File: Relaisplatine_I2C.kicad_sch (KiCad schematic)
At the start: 74 parts, among them J1 K, J1.1 G1-K, J1.1a1001 G1-J, J1.1a1002 G1-K, J1.1a1003 G1-K, J1.1a1004 G1-K, J1.1a1005 G1-K, J1.1a1006 G1-K, J1.1a1007 G1-K, J1.2 G1-J, J1.2a1001 G1-K, J1.2a1002 G1-J, J1.2a1003 G1-J, J1.2a1004 G1-J, J1.2a1005 G1-J, J1.2a1006 G1-J, J1.2a1007 G1-J, J10 I²C, J11 Relais-Power, J12 Int, J2 J, J2.1 G2-K, J2.1a1001 G1-J, J2.2 G2-J, J2.2a1001 G2-K, J3.1 G3-K, J3.2 G3-J, J4.1 G4-K, J4.2 G4-J, J5.1 G5-K, J5.2 G5-J, J6.1 G6-K, J6.2 G6-J, J7.1 G7-K, J7.2 G7-J, J8.1 G8-K, J8.2 G8-J, U1 ULN2803A, U2 PCF8574

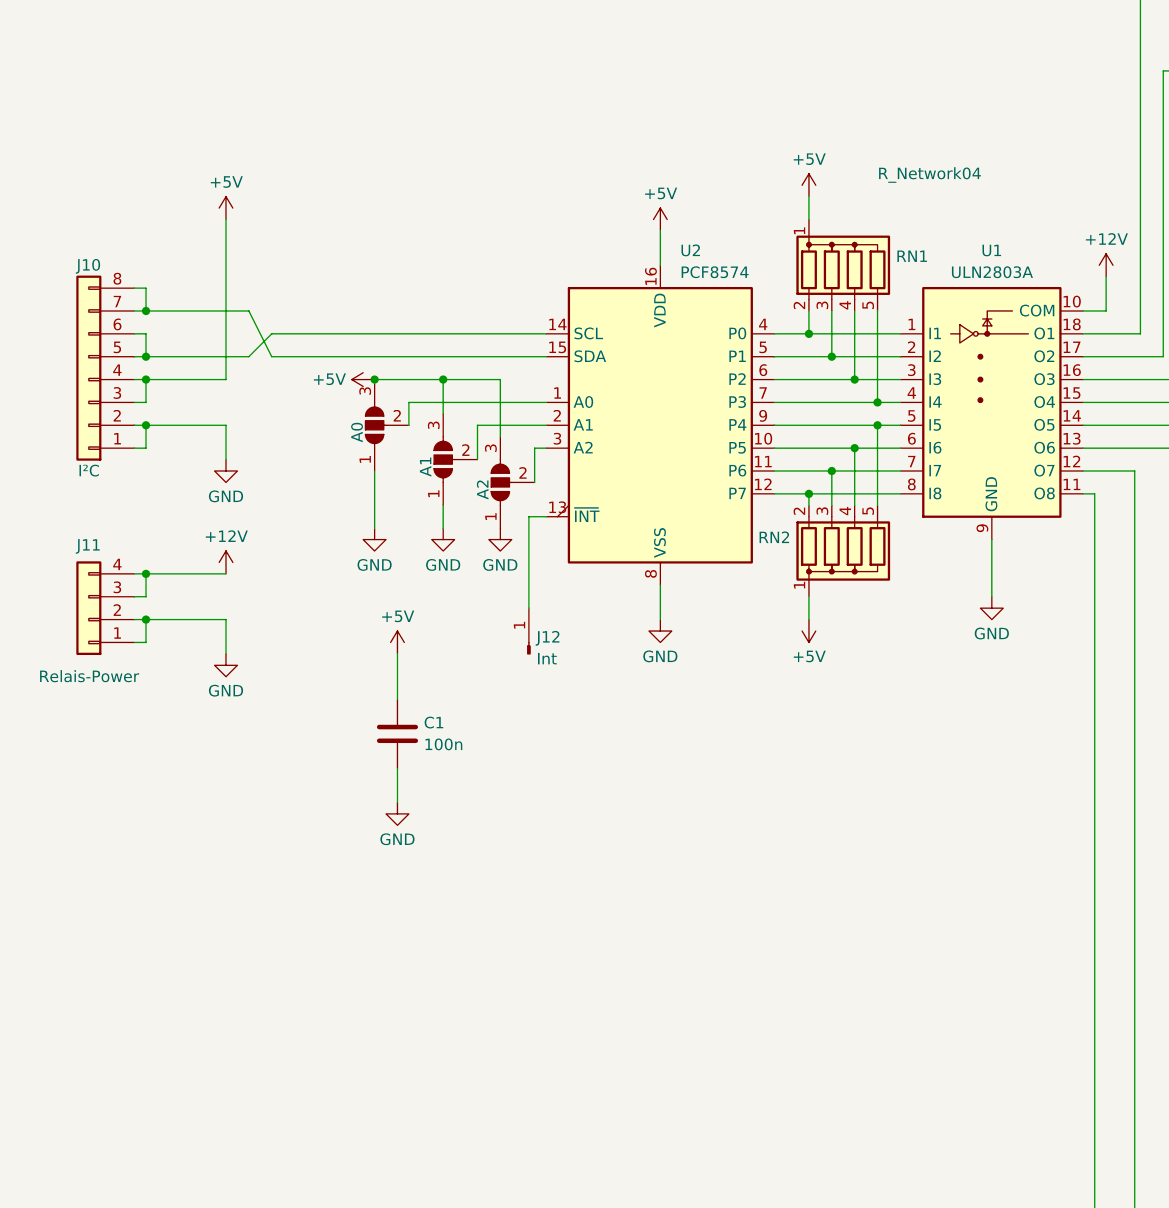
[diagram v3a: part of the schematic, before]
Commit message: Power-LEDs für 5V und 12V hinzugefügt
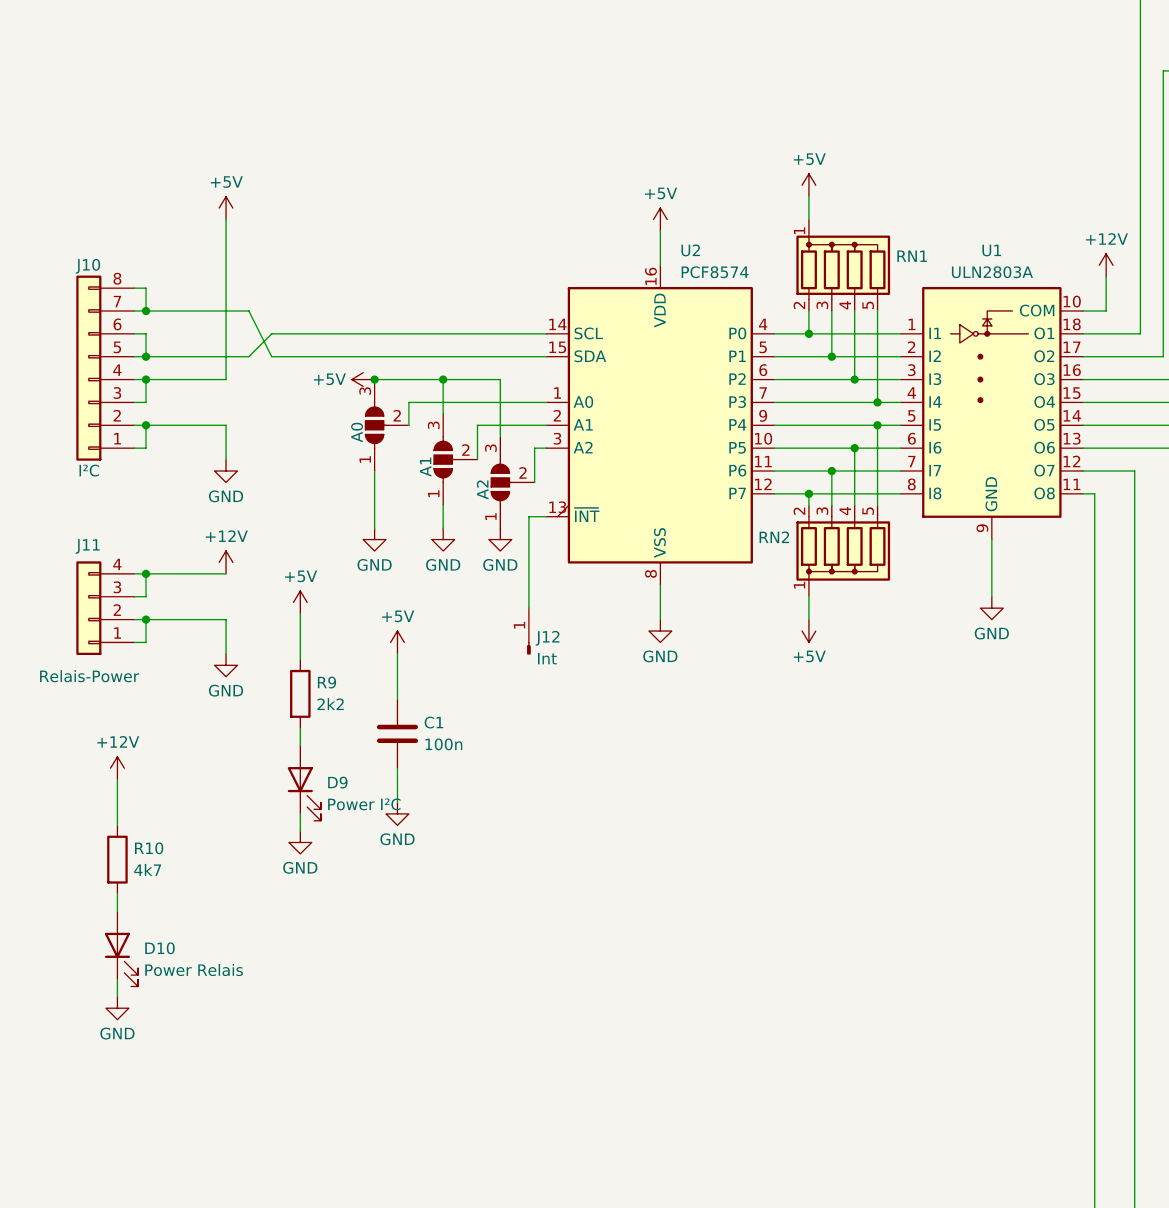
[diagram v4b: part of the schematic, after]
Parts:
- added D10: Power Relais, LED_SMD:LED_0805_2012Metric_Pad1.15x1.40mm_HandSolder, symbol Device:LED
- added D9: Power I²C, LED_SMD:LED_0805_2012Metric_Pad1.15x1.40mm_HandSolder, symbol Device:LED
- added R10: 4k7, Resistor_SMD:R_0805_2012Metric_Pad1.20x1.40mm_HandSolder, symbol Device:R
- added R9: 2k2, Resistor_SMD:R_0805_2012Metric_Pad1.20x1.40mm_HandSolder, symbol Device:R
- RN1: value R_Network04 -> RN1
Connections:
- net +12V: now also R10.1
- net +5V: now also R9.1
- net GND: now also D10.1 (K), D9.1 (K)
- new net: D9.2 (A), R9.2
- new net: D10.2 (A), R10.2
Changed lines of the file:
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@@
+    (stroke (width 0) (type default))
+  )
+  (wire (pts (xy 34.925 191.135) (xy 34.925 193.04))
     (stroke (width 0) (type default))
   )
@@
     (stroke (width 0) (type default))
   )
+  (wire (pts (xy 34.925 181.61) (xy 34.925 183.515))
+    (stroke (width 0) (type default))
+  )
   (wire (pts (xy 165.735 247.65) (xy 165.735 281.94))
     (stroke (width 0) (type default))
@@
     (stroke (width 0) (type default))
   )
+  (wire (pts (xy 34.925 168.91) (xy 34.925 173.99))
+    (stroke (width 0) (type default))
+  )
   (wire (pts (xy 67.31 129.54) (xy 67.31 127))
     (stroke (width 0) (type default))
   )
+  (wire (pts (xy 55.245 150.495) (xy 55.245 155.575))
+    (stroke (width 0) (type default))
+  )
   (wire (pts (xy 143.51 295.91) (xy 143.51 299.72))
     (stroke (width 0) (type default))
@@
     (stroke (width 0) (type default))
   )
+  (wire (pts (xy 55.245 163.195) (xy 55.245 165.1))
+    (stroke (width 0) (type default))
+  )
   (wire (pts (xy 187.96 158.75) (xy 186.69 158.75))
     (stroke (width 0) (type default))
@@
   )
   (wire (pts (xy 187.96 227.33) (xy 186.69 227.33))
+    (stroke (width 0) (type default))
+  )
+  (wire (pts (xy 55.245 172.72) (xy 55.245 174.625))
     (stroke (width 0) (type default))
   )
@@
         (path "/07762166-ac5c-4527-9a95-bcec2ea66161"
           (reference "J1") (unit 1)
+        )
+      )
+    )
+  )
+  (symbol (lib_id "power:+5V") (at 55.245 150.495 0) (unit 1)
+    (in_bom yes) (on_board yes) (dnp no) (fields_autoplaced)
+    (property "Reference" "#PWR01020" (at 55.245 154.305 0)
+      (effects (font (size 1.27 1.27)) hide)
+    )
+    (property "Value" "+5V" (at 55.245 146.3619 0)
+      (effects (font (size 1.27 1.27)))
+    )
+    (property "Footprint" "" (at 55.245 150.495 0)
+      (effects (font (size 1.27 1.27)) hide)
+    )
+    (property "Datasheet" "" (at 55.245 150.495 0)
+      (effects (font (size 1.27 1.27)) hide)
+    )
+    (pin "1")
+    (instances
+      (project "Relaisplatine_I2C"
+        (path "/064c37a5-963a-4246-bd9f-fec8b6e7897e"
+          (reference "#PWR01020") (unit 1)
         )
       )
@@
     )
   )
+  (symbol (lib_id "Device:R") (at 55.245 159.385 0) (unit 1)
+    (in_bom yes) (on_board yes) (dnp no) (fields_autoplaced)
+    (property "Reference" "R9" (at 57.023 158.1729 0)
+      (effects (font (size 1.27 1.27)) (justify left))
+    )
+    (property "Value" "2k2" (at 57.023 160.5971 0)
+      (effects (font (size 1.27 1.27)) (justify left))
+    )
+    (property "Footprint" "Resistor_SMD:R_0805_2012Metric_Pad1.20x1.40mm_HandSolder" (at 53.467 159.385 90)
+      (effects (font (size 1.27 1.27)) hide)
+    )
+    (property "Datasheet" "~" (at 55.245 159.385 0)
+      (effects (font (size 1.27 1.27)) hide)
+    )
+    (pin "2")
+    (pin "1")
+    (instances
+      (project "Relaisplatine_I2C"
+        (path "/064c37a5-963a-4246-bd9f-fec8b6e7897e"
+          (reference "R9") (unit 1)
+        )
+      )
+    )
+  )
   (symbol (lib_id "Connector_Generic:Conn_01x01") (at 198.12 68.58 0) (unit 1)
     (in_bom yes) (on_board yes) (dnp no)
@@
     )
   )
+  (symbol (lib_id "Device:LED") (at 34.925 187.325 90) (unit 1)
+    (in_bom yes) (on_board yes) (dnp no) (fields_autoplaced)
+    (property "Reference" "D10" (at 37.846 187.7004 90)
+      (effects (font (size 1.27 1.27)) (justify right))
+    )
+    (property "Value" "Power Relais" (at 37.846 190.1246 90)
+      (effects (font (size 1.27 1.27)) (justify right))
+    )
+    (property "Footprint" "LED_SMD:LED_0805_2012Metric_Pad1.15x1.40mm_HandSolder" (at 34.925 187.325 0)
+      (effects (font (size 1.27 1.27)) hide)
+    )
+    (property "Datasheet" "~" (at 34.925 187.325 0)
+      (effects (font (size 1.27 1.27)) hide)
+    )
+    (pin "2")
+    (pin "1")
+    (instances
+      (project "Relaisplatine_I2C"
+        (path "/064c37a5-963a-4246-bd9f-fec8b6e7897e"
+          (reference "D10") (unit 1)
+        )
+      )
+    )
+  )
+  (symbol (lib_id "power:GND") (at 55.245 174.625 0) (unit 1)
+    (in_bom yes) (on_board yes) (dnp no) (fields_autoplaced)
+    (property "Reference" "#PWR01021" (at 55.245 180.975 0)
+      (effects (font (size 1.27 1.27)) hide)
+    )
+    (property "Value" "GND" (at 55.245 178.7581 0)
+      (effects (font (size 1.27 1.27)))
+    )
+    (property "Footprint" "" (at 55.245 174.625 0)
+      (effects (font (size 1.27 1.27)) hide)
+    )
+    (property "Datasheet" "" (at 55.245 174.625 0)
+      (effects (font (size 1.27 1.27)) hide)
+    )
+    (pin "1")
+    (instances
+      (project "Relaisplatine_I2C"
+        (path "/064c37a5-963a-4246-bd9f-fec8b6e7897e"
+          (reference "#PWR01021") (unit 1)
+        )
+      )
+    )
+  )
   (symbol (lib_id "Device:LED") (at 152.4 303.53 270) (unit 1)
     (in_bom yes) (on_board yes) (dnp no)
@@
       (effects (font (size 1.27 1.27)) (justify left))
     )
-    (property "Value" "R_Network04" (at 119.38 101.6 0)
-      (effects (font (size 1.27 1.27)) (justify left))
+    (property "Value" "RN1" (at 119.38 101.6 0)
+      (effects (font (size 1.27 1.27)) (justify left) hide)
     )
     (property "Footprint" "Resistor_THT:R_Array_SIP5" (at 123.825 111.76 90)
@@
         (path "/064c37a5-963a-4246-bd9f-fec8b6e7897e"
           (reference "#PWR01019") (unit 1)
+        )
+      )
+    )
+  )
+  (symbol (lib_id "Device:LED") (at 55.245 168.91 90) (unit 1)
+    (in_bom yes) (on_board yes) (dnp no) (fields_autoplaced)
+    (property "Reference" "D9" (at 58.166 169.2854 90)
+      (effects (font (size 1.27 1.27)) (justify right))
+    )
+    (property "Value" "Power I²C" (at 58.166 171.7096 90)
+      (effects (font (size 1.27 1.27)) (justify right))
+    )
+    (property "Footprint" "LED_SMD:LED_0805_2012Metric_Pad1.15x1.40mm_HandSolder" (at 55.245 168.91 0)
+      (effects (font (size 1.27 1.27)) hide)
+    )
+    (property "Datasheet" "~" (at 55.245 168.91 0)
+      (effects (font (size 1.27 1.27)) hide)
+    )
+    (pin "2")
+    (pin "1")
+    (instances
+      (project "Relaisplatine_I2C"
+        (path "/064c37a5-963a-4246-bd9f-fec8b6e7897e"
+          (reference "D9") (unit 1)
         )
       )
@@
     )
   )
+  (symbol (lib_id "Device:R") (at 34.925 177.8 0) (unit 1)
+    (in_bom yes) (on_board yes) (dnp no) (fields_autoplaced)
+    (property "Reference" "R10" (at 36.703 176.5879 0)
+      (effects (font (size 1.27 1.27)) (justify left))
+    )
+    (property "Value" "4k7" (at 36.703 179.0121 0)
+      (effects (font (size 1.27 1.27)) (justify left))
+    )
+    (property "Footprint" "Resistor_SMD:R_0805_2012Metric_Pad1.20x1.40mm_HandSolder" (at 33.147 177.8 90)
+      (effects (font (size 1.27 1.27)) hide)
+    )
+    (property "Datasheet" "~" (at 34.925 177.8 0)
+      (effects (font (size 1.27 1.27)) hide)
+    )
+    (pin "2")
+    (pin "1")
+    (instances
+      (project "Relaisplatine_I2C"
+        (path "/064c37a5-963a-4246-bd9f-fec8b6e7897e"
+          (reference "R10") (unit 1)
+        )
+      )
+    )
+  )
   (symbol (lib_id "Connector_Generic:Conn_01x01") (at 198.12 137.16 0) (unit 1)
     (in_bom yes) (on_board yes) (dnp no)
@@
     )
   )
+  (symbol (lib_id "power:GND") (at 34.925 193.04 0) (unit 1)
+    (in_bom yes) (on_board yes) (dnp no) (fields_autoplaced)
+    (property "Reference" "#PWR01023" (at 34.925 199.39 0)
+      (effects (font (size 1.27 1.27)) hide)
+    )
+    (property "Value" "GND" (at 34.925 197.1731 0)
+      (effects (font (size 1.27 1.27)))
+    )
+    (property "Footprint" "" (at 34.925 193.04 0)
+      (effects (font (size 1.27 1.27)) hide)
+    )
+    (property "Datasheet" "" (at 34.925 193.04 0)
+      (effects (font (size 1.27 1.27)) hide)
+    )
+    (pin "1")
+    (instances
+      (project "Relaisplatine_I2C"
+        (path "/064c37a5-963a-4246-bd9f-fec8b6e7897e"
+          (reference "#PWR01023") (unit 1)
+        )
+      )
+    )
+  )
   (symbol (lib_id "Connector_Generic:Conn_01x01") (at 204.47 73.66 0) (unit 1)
     (in_bom yes) (on_board yes) (dnp no)
@@
         )
       )
+    )
+  )
+  (symbol (lib_id "power:+12V") (at 34.925 168.91 0) (unit 1)
+    (in_bom yes) (on_board yes) (dnp no) (fields_autoplaced)
+    (property "Reference" "#PWR01022" (at 34.925 172.72 0)
+      (effects (font (size 1.27 1.27)) hide)
+    )
+    (property "Value" "+12V" (at 34.925 164.7769 0)
+      (effects (font (size 1.27 1.27)))
+    )
+    (property "Footprint" "" (at 34.925 168.91 0)
+      (effects (font (size 1.27 1.27)) hide)
+    )
+    (property "Datasheet" "" (at 34.925 168.91 0)
+      (effects (font (size 1.27 1.27)) hide)
+    )
+    (pin "1")
+    (instances
+      (project "Relaisplatine_I2C"
+        (path "/064c37a5-963a-4246-bd9f-fec8b6e7897e"
+          (reference "#PWR01022") (unit 1)
+        )
+      )

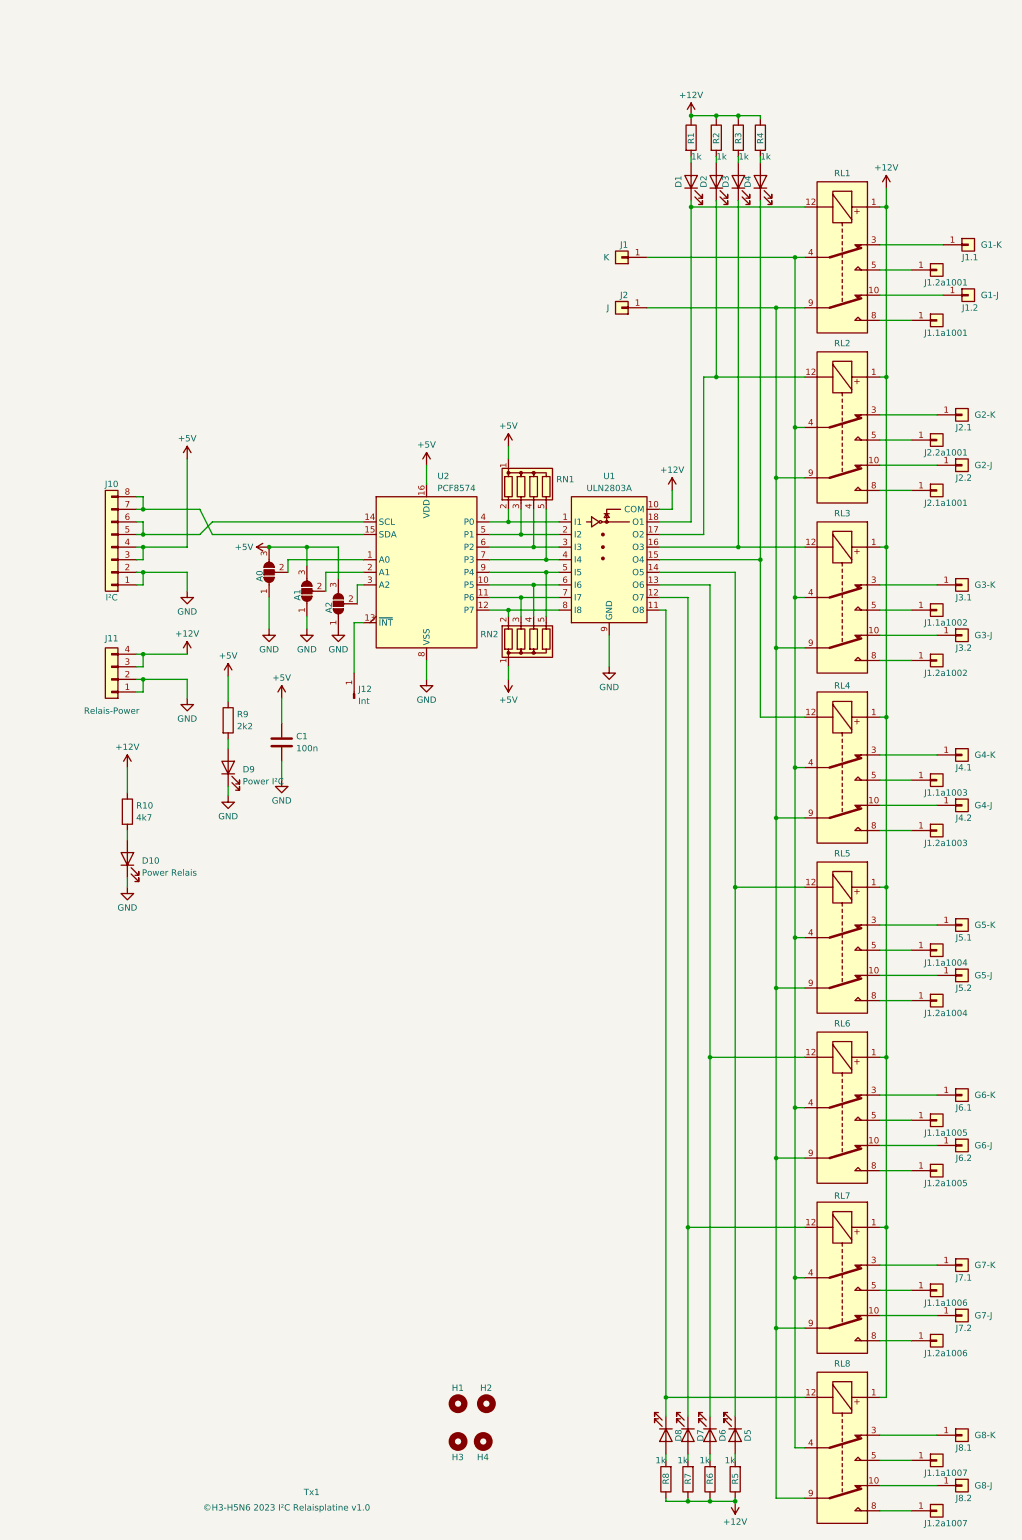
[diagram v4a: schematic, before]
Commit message: Revision als Feld, Widerstand der Ralais-LEDs auf 10k gesetzt
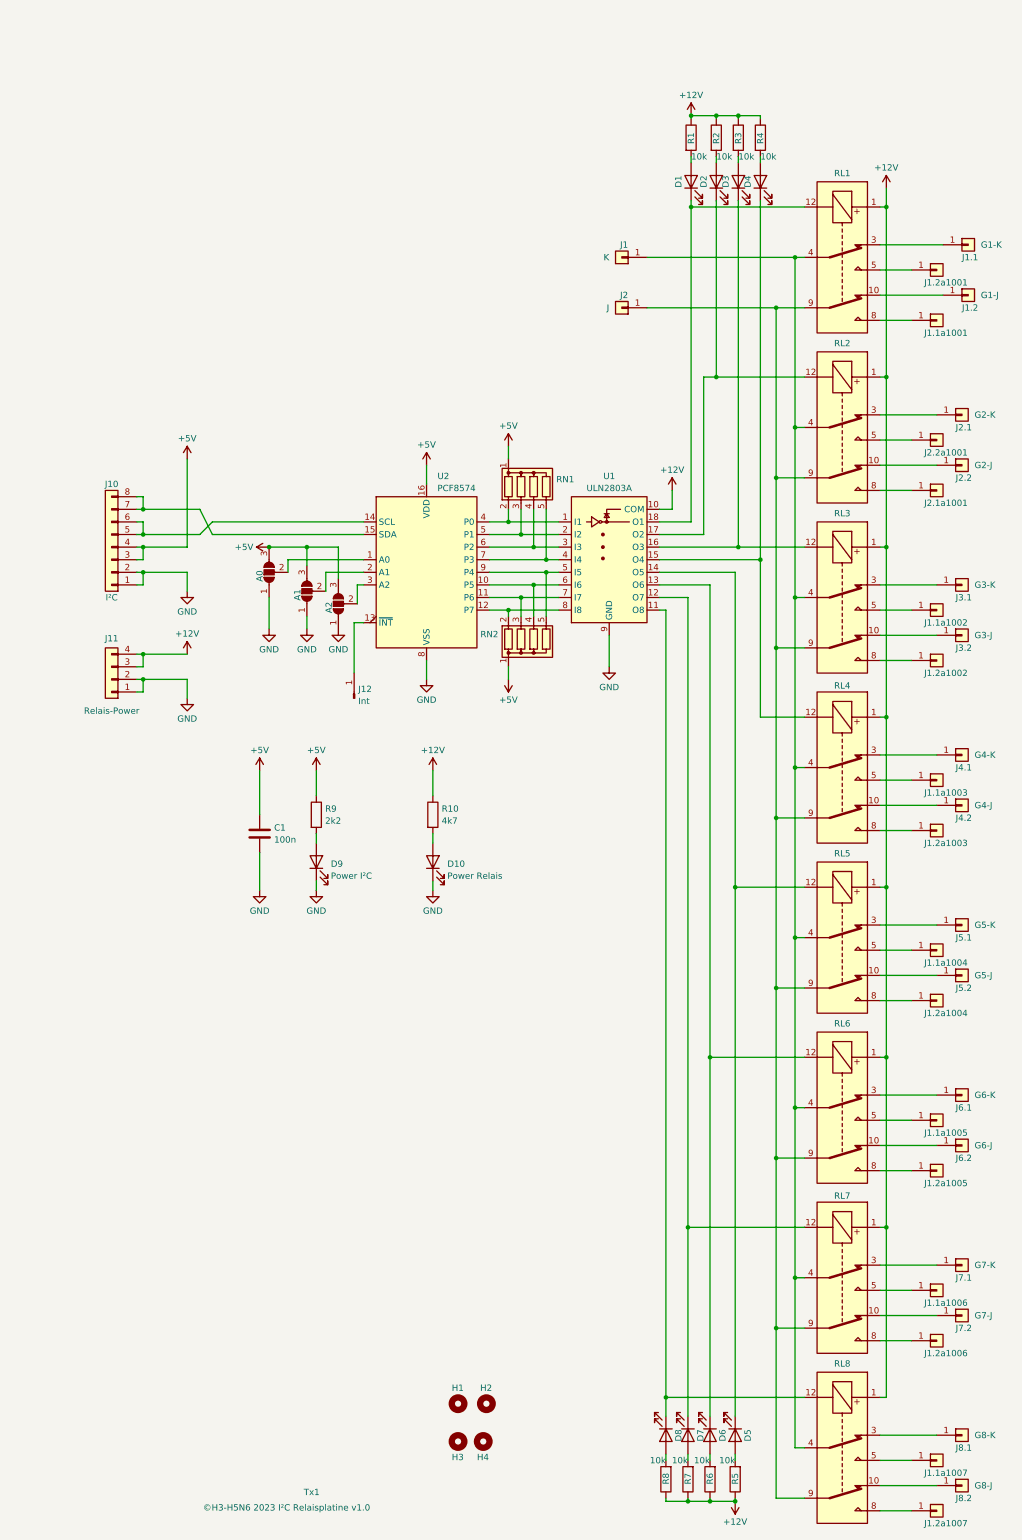
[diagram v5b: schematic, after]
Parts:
- R1, R2, R3, R4, R5, R6, R7, R8: value 1k -> 10k; Quelle (none) -> Resistor_SMD:R_0805_2012Metric_Pad1.20x1.40mm_HandSolder
- Tx1: value ©H3-H5N6 2023 I²C Relaisplatine v1.0 -> ©H3-H5N6 2023 I²C Relaisplatine ${REVISION}
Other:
- title: I²C 8-fach Railsplatine -> I²C 8-fach Relaisplatine
- moved on the sheet: C1, D10, D9, R10, R9
